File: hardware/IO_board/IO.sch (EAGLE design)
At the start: 66 parts, among them IC1 MAX232, IC10 74HCT245DW, IC4 74HCT139N, IC5 74AC06N, IC7 MAX232, IC8 74HCT245DW, IC9 74HCT245DW, J1 DIN5, X2 CRYSTALS-NOGND-CFPX-217, X4 736880-49

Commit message: Audio circuit added to I/O board
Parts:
- added C33: (no value), rcl:CPOL-EUE2-4
- added C34: 100N, rcl:C-EUC0603
- added IC11: 74LVC1G08DBV, 74xx-little-de:74LVC1G08DBV
- added R14: (no value), rcl:R-EU_0204/7
- added R15: (no value), rcl:R-EU_R0603
- added T1: BC847, transistor:BC847
- R1: device rcl:R-EU_0204/7 -> rcl:R-EU_R0603
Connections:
- new net N$26: R1.2, T1.B
- new net N$27: R15.1, T1.C
- new net N$30: C33.-, X4.2
- new net N$40: C33.+, R14.1, R15.2
- net BOARD_ENABLE: now also IC11A.O
- net CS_0: now also IC11A.I0
- net CS_2: now also IC11A.I1
- net GND: now also C34.2, T1.E, X4.1
- net VCC: now also C34.1, R14.2
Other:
- moved on the sheet: X4
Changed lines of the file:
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@@
 <part name="R11" library="rcl" deviceset="R-EU_" device="R0603"/>
 <part name="X4" library="con-conrad" deviceset="736880-49" device=""/>
-<part name="R1" library="rcl" deviceset="R-EU_" device="0204/7"/>
+<part name="R1" library="rcl" deviceset="R-EU_" device="R0603"/>
+<part name="IC11" library="74xx-little-de" deviceset="74*1G08" device="DBV" technology="LVC"/>
+<part name="T1" library="transistor" deviceset="BC847" device=""/>
+<part name="GND16" library="supply1" deviceset="GND" device=""/>
+<part name="R14" library="rcl" deviceset="R-EU_" device="0204/7"/>
+<part name="C33" library="rcl" deviceset="CPOL-EU" device="E2-4"/>
+<part name="GND18" library="supply1" deviceset="GND" device=""/>
+<part name="R15" library="rcl" deviceset="R-EU_" device="R0603"/>
+<part name="C34" library="rcl" deviceset="C-EU" device="C0603" value="100N"/>
 </parts>
 <sheets>
@@
 <instance part="R6" gate="G$1" x="99.06" y="332.74" rot="R90"/>
 <instance part="R11" gate="G$1" x="93.98" y="332.74" rot="R90"/>
-<instance part="X4" gate="G$1" x="73.66" y="363.22" rot="MR0"/>
+<instance part="X4" gate="G$1" x="182.88" y="322.58" rot="MR0"/>
 <instance part="R1" gate="G$1" x="149.86" y="322.58"/>
+<instance part="IC11" gate="A" x="111.76" y="-96.52"/>
+<instance part="T1" gate="G$1" x="160.02" y="322.58"/>
+<instance part="GND16" gate="1" x="162.56" y="312.42"/>
+<instance part="R14" gate="G$1" x="162.56" y="350.52" rot="R90"/>
+<instance part="C33" gate="G$1" x="167.64" y="342.9" rot="R90"/>
+<instance part="GND18" gate="1" x="175.26" y="312.42"/>
+<instance part="R15" gate="G$1" x="162.56" y="335.28" rot="R90"/>
+<instance part="C34" gate="G$1" x="-63.5" y="231.14"/>
 </instances>
 <busses>
@@
 <wire x1="-71.12" y1="223.52" x2="-71.12" y2="226.06" width="0.1524" layer="91"/>
 <junction x="-78.74" y="223.52"/>
+<pinref part="C34" gate="G$1" pin="2"/>
+<wire x1="-71.12" y1="223.52" x2="-63.5" y2="223.52" width="0.1524" layer="91"/>
+<wire x1="-63.5" y1="223.52" x2="-63.5" y2="226.06" width="0.1524" layer="91"/>
+<junction x="-71.12" y="223.52"/>
 </segment>
 <segment>
@@
 <junction x="261.62" y="27.94"/>
 </segment>
+<segment>
+<pinref part="T1" gate="G$1" pin="E"/>
+<pinref part="GND16" gate="1" pin="GND"/>
+<wire x1="162.56" y1="314.96" x2="162.56" y2="317.5" width="0.1524" layer="91"/>
+</segment>
+<segment>
+<pinref part="GND18" gate="1" pin="GND"/>
+<wire x1="180.34" y1="320.04" x2="175.26" y2="320.04" width="0.1524" layer="91"/>
+<wire x1="175.26" y1="320.04" x2="175.26" y2="314.96" width="0.1524" layer="91"/>
+<pinref part="X4" gate="G$1" pin="1"/>
+</segment>
 </net>
 <net name="D0" class="0">
@@
 <label x="-91.44" y="-68.58" size="1.4224" layer="95" rot="R180" xref="yes"/>
 </segment>
+<segment>
+<pinref part="IC11" gate="A" pin="I0"/>
+<wire x1="106.68" y1="-93.98" x2="99.06" y2="-93.98" width="0.1524" layer="91"/>
+<label x="99.06" y="-93.98" size="1.4224" layer="95" rot="R180" xref="yes"/>
+</segment>
 </net>
 <net name="CS_1" class="0">
@@
 <wire x1="99.06" y1="-73.66" x2="93.98" y2="-73.66" width="0.1524" layer="91"/>
 <label x="93.98" y="-73.66" size="1.4224" layer="95" rot="R180" xref="yes"/>
+</segment>
+<segment>
+<pinref part="IC11" gate="A" pin="I1"/>
+<wire x1="106.68" y1="-99.06" x2="99.06" y2="-99.06" width="0.1524" layer="91"/>
+<label x="99.06" y="-99.06" size="1.4224" layer="95" rot="R180" xref="yes"/>
 </segment>
 </net>
@@
 <wire x1="-71.12" y1="236.22" x2="-71.12" y2="233.68" width="0.1524" layer="91"/>
 <junction x="-78.74" y="236.22"/>
+<pinref part="C34" gate="G$1" pin="1"/>
+<wire x1="-71.12" y1="236.22" x2="-63.5" y2="236.22" width="0.1524" layer="91"/>
+<wire x1="-63.5" y1="236.22" x2="-63.5" y2="233.68" width="0.1524" layer="91"/>
+<junction x="-71.12" y="236.22"/>
 </segment>
 <segment>
@@
 <pinref part="R6" gate="G$1" pin="2"/>
 <wire x1="99.06" y1="340.36" x2="99.06" y2="337.82" width="0.1524" layer="91"/>
+</segment>
+<segment>
+<pinref part="R14" gate="G$1" pin="2"/>
+<wire x1="162.56" y1="355.6" x2="162.56" y2="358.14" width="0.1524" layer="91"/>
 </segment>
 </net>
@@
 <pinref part="IC8" gate="A" pin="DIR"/>
 <wire x1="264.16" y1="58.42" x2="259.08" y2="58.42" width="0.1524" layer="91"/>
+<label x="259.08" y="58.42" size="1.4224" layer="95" rot="R180" xref="yes"/>
 </segment>
 </net>
@@
 <pinref part="IC8" gate="A" pin="G"/>
 <wire x1="264.16" y1="55.88" x2="259.08" y2="55.88" width="0.1524" layer="91"/>
+<label x="259.08" y="55.88" size="1.4224" layer="95" rot="R180" xref="yes"/>
+</segment>
+<segment>
+<pinref part="IC11" gate="A" pin="O"/>
+<wire x1="119.38" y1="-96.52" x2="127" y2="-96.52" width="0.1524" layer="91"/>
+<label x="127" y="-96.52" size="1.4224" layer="95" xref="yes"/>
 </segment>
 </net>
@@
 </segment>
 </net>
+<net name="N$26" class="0">
+<segment>
+<pinref part="R1" gate="G$1" pin="2"/>
+<wire x1="157.48" y1="322.58" x2="154.94" y2="322.58" width="0.1524" layer="91"/>
+<pinref part="T1" gate="G$1" pin="B"/>
+</segment>
+</net>
+<net name="N$27" class="0">
+<segment>
+<pinref part="T1" gate="G$1" pin="C"/>
+<pinref part="R15" gate="G$1" pin="1"/>
+<wire x1="162.56" y1="330.2" x2="162.56" y2="327.66" width="0.1524" layer="91"/>
+</segment>
+</net>
+<net name="N$30" class="0">
+<segment>
+<pinref part="C33" gate="G$1" pin="-"/>
+<wire x1="172.72" y1="342.9" x2="175.26" y2="342.9" width="0.1524" layer="91"/>
+<wire x1="180.34" y1="322.58" x2="175.26" y2="322.58" width="0.1524" layer="91"/>
+<wire x1="175.26" y1="322.58" x2="175.26" y2="342.9" width="0.1524" layer="91"/>
+<pinref part="X4" gate="G$1" pin="2"/>
+</segment>
+</net>
+<net name="N$40" class="0">
+<segment>
+<pinref part="R14" gate="G$1" pin="1"/>
+<pinref part="R15" gate="G$1" pin="2"/>
+<wire x1="162.56" y1="340.36" x2="162.56" y2="342.9" width="0.1524" layer="91"/>
+<pinref part="C33" gate="G$1" pin="+"/>
+<wire x1="162.56" y1="342.9" x2="162.56" y2="345.44" width="0.1524" layer="91"/>
+<wire x1="165.1" y1="342.9" x2="162.56" y2="342.9" width="0.1524" layer="91"/>
+<junction x="162.56" y="342.9"/>
+</segment>
+</net>

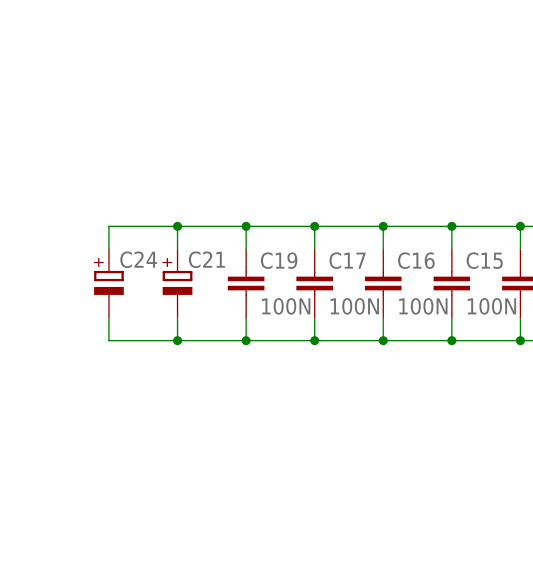
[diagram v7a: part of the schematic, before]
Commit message: Capacitors added to I/O board
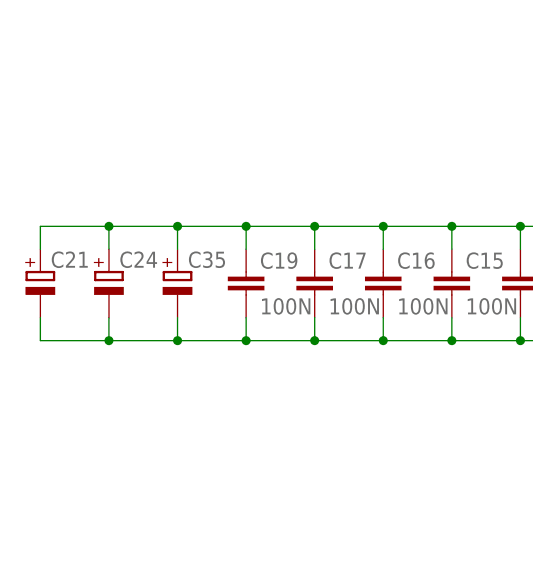
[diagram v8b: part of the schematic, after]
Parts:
- added C35: (no value), rcl:CPOL-EUE5-10.5
- C21: device rcl:CPOL-EUE3.5-8 -> rcl:CPOL-EUSMCB
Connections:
- net GND: now also C35.-
- net VCC: now also C35.+
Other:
- moved on the sheet: C21
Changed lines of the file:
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@@
 <part name="JP3" library="pinhead" deviceset="PINHD-1X2" device="/90"/>
 <part name="GND14" library="supply1" deviceset="GND" device=""/>
-<part name="C21" library="rcl" deviceset="CPOL-EU" device="E3.5-8"/>
 <part name="C24" library="rcl" deviceset="CPOL-EU" device="SMCB"/>
 <part name="IC4" library="74xx-eu" deviceset="74*139" device="N" technology="HCT"/>
@@
 <part name="R15" library="rcl" deviceset="R-EU_" device="R0603"/>
 <part name="C34" library="rcl" deviceset="C-EU" device="C0603" value="100N"/>
+<part name="C35" library="rcl" deviceset="CPOL-EU" device="E5-10.5"/>
+<part name="C21" library="rcl" deviceset="CPOL-EU" device="SMCB"/>
 </parts>
 <sheets>
@@
 <instance part="JP3" gate="G$1" x="-43.18" y="226.06"/>
 <instance part="GND14" gate="1" x="-53.34" y="218.44"/>
-<instance part="C21" gate="G$1" x="-177.8" y="231.14"/>
 <instance part="C24" gate="G$1" x="-185.42" y="231.14"/>
 <instance part="IC4" gate="A" x="53.34" y="-68.58"/>
@@
 <instance part="R15" gate="G$1" x="162.56" y="335.28" rot="R90"/>
 <instance part="C34" gate="G$1" x="-63.5" y="231.14"/>
+<instance part="C35" gate="G$1" x="-177.8" y="231.14"/>
+<instance part="C21" gate="G$1" x="-193.04" y="231.14"/>
 </instances>
 <busses>
@@
 <wire x1="-170.18" y1="223.52" x2="-170.18" y2="226.06" width="0.1524" layer="91"/>
 <junction x="-162.56" y="223.52"/>
-<pinref part="C21" gate="G$1" pin="-"/>
 <wire x1="-170.18" y1="223.52" x2="-177.8" y2="223.52" width="0.1524" layer="91"/>
 <wire x1="-177.8" y1="223.52" x2="-177.8" y2="226.06" width="0.1524" layer="91"/>
@@
 <wire x1="-63.5" y1="223.52" x2="-63.5" y2="226.06" width="0.1524" layer="91"/>
 <junction x="-71.12" y="223.52"/>
+<pinref part="C35" gate="G$1" pin="-"/>
+<pinref part="C21" gate="G$1" pin="-"/>
+<wire x1="-185.42" y1="223.52" x2="-193.04" y2="223.52" width="0.1524" layer="91"/>
+<wire x1="-193.04" y1="223.52" x2="-193.04" y2="226.06" width="0.1524" layer="91"/>
+<junction x="-185.42" y="223.52"/>
 </segment>
 <segment>
@@
 <wire x1="-170.18" y1="236.22" x2="-170.18" y2="233.68" width="0.1524" layer="91"/>
 <junction x="-162.56" y="236.22"/>
-<pinref part="C21" gate="G$1" pin="+"/>
 <wire x1="-170.18" y1="236.22" x2="-177.8" y2="236.22" width="0.1524" layer="91"/>
 <wire x1="-177.8" y1="236.22" x2="-177.8" y2="233.68" width="0.1524" layer="91"/>
@@
 <wire x1="-63.5" y1="236.22" x2="-63.5" y2="233.68" width="0.1524" layer="91"/>
 <junction x="-71.12" y="236.22"/>
-</segment>
-<segment>
+<pinref part="C35" gate="G$1" pin="+"/>
+<pinref part="C21" gate="G$1" pin="+"/>
+<wire x1="-185.42" y1="236.22" x2="-193.04" y2="236.22" width="0.1524" layer="91"/>
+<wire x1="-193.04" y1="236.22" x2="-193.04" y2="233.68" width="0.1524" layer="91"/>
+<junction x="-185.42" y="236.22"/>
+</segment>
+<segment>
